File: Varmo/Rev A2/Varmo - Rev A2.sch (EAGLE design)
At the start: 110 parts, among them J1 22-05-7028-02, J2 22-05-7028-02, J3 22-05-7038-03, J4 22-05-7038-03, J5 22-05-7038-03, J6 22-05-7038-03, J7 22-05-7058-05, J9 22-05-7038-03, T1 MMBT2222AL, U1 LT1813CS8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

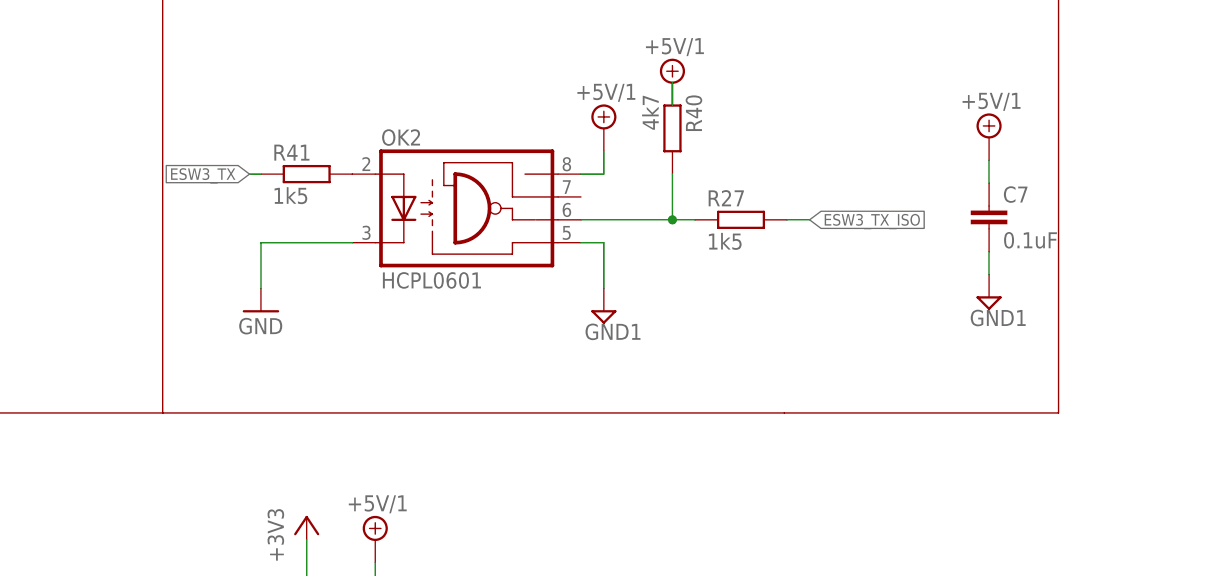
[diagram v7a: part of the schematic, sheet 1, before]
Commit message: Replace the HCPL0601 with the HCPL0201 optocoupler
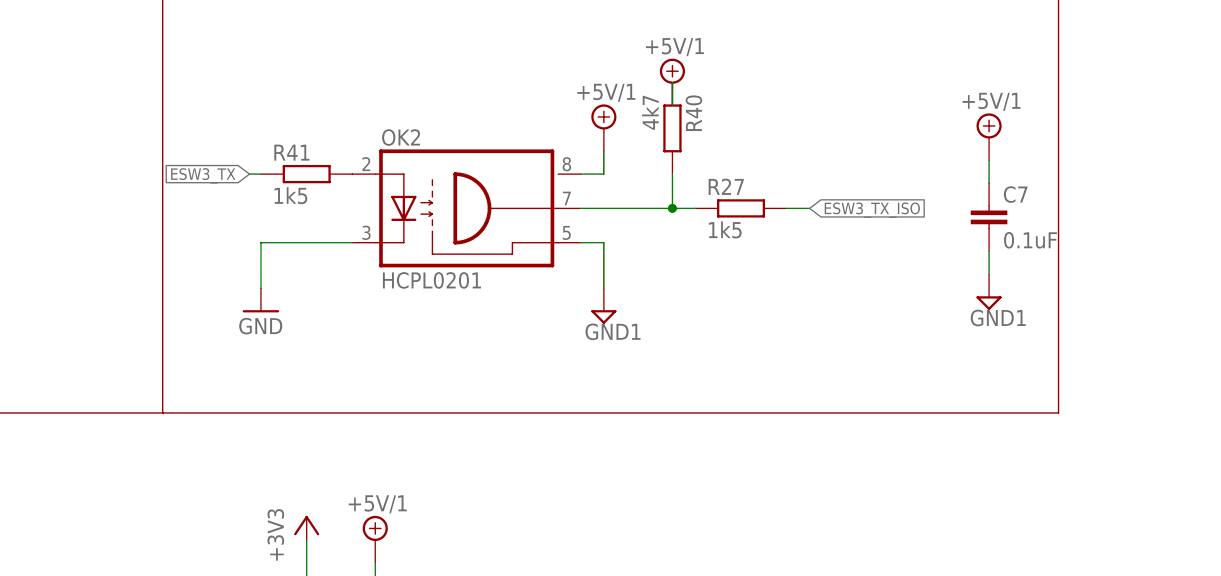
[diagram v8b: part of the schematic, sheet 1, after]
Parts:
- OK2: value HCPL0601 -> HCPL0201; device optocoupler:HCPL0601 -> optocoupler:HCPL0201
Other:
- moved on the sheet: R27
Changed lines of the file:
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@@
 <?xml version="1.0" encoding="utf-8"?>
 <!DOCTYPE eagle SYSTEM "eagle.dtd">
-<eagle version="7.5.0">
+<eagle version="7.6.0">
 <drawing>
 <settings>
@@
 <setting verticaltext="up"/>
 </settings>
-<grid distance="0.1" unitdist="inch" unit="inch" style="lines" multiple="1" display="no" altdistance="0.01" altunitdist="inch" altunit="inch"/>
+<grid distance="0.1" unitdist="inch" unit="inch" style="lines" multiple="1" display="no" altdistance="0.05" altunitdist="inch" altunit="inch"/>
 <layers>
 <layer number="1" name="Top" color="4" fill="1" visible="no" active="no"/>
@@
 </part>
 <part name="SUPPLY59" library="supply2" deviceset="+5V/1" device=""/>
-<part name="OK2" library="optocoupler" deviceset="HCPL0601" device=""/>
+<part name="OK2" library="optocoupler" deviceset="HCPL0201" device=""/>
 <part name="R41" library="rcl" deviceset="R-EU_" device="R0603" value="1k5">
 <attribute name="MF" value=""/>
@@
 <text x="113.64" y="197.58" size="1.778" layer="97">SIGNAL ISOLATION</text>
 <text x="105.38" y="252.38" size="1.778" layer="97">DC-DC convertor</text>
-<wire x1="169.92" y1="103" x2="100.84" y2="103" width="0.1524" layer="94"/>
+<wire x1="200.38" y1="103" x2="100.84" y2="103" width="0.1524" layer="94"/>
 <wire x1="100.84" y1="103" x2="3.746" y2="103" width="0.1524" layer="94"/>
 <wire x1="100.84" y1="103" x2="100.84" y2="202" width="0.1524" layer="94"/>
@@
 <wire x1="200.38" y1="202" x2="200.38" y2="182.92" width="0.1524" layer="94"/>
 <wire x1="200.38" y1="182.92" x2="200.38" y2="103" width="0.1524" layer="94"/>
-<wire x1="200.38" y1="103" x2="169.92" y2="103" width="0.1524" layer="94"/>
 <wire x1="383.492" y1="182.92" x2="200.38" y2="182.92" width="0.1524" layer="94"/>
 <text x="113.64" y="197.58" size="1.778" layer="97">SIGNAL ISOLATION</text>
@@
 </instance>
 <instance part="SUPPLY59" gate="G$1" x="157.48" y="139.7"/>
-<instance part="OK2" gate="A" x="134.62" y="124.46"/>
+<instance part="OK2" gate="G$1" x="134.62" y="124.46"/>
 <instance part="R41" gate="G$1" x="116.84" y="129.54">
 <attribute name="OC_NEWARK" x="116.84" y="129.54" size="1.778" layer="96" rot="R90" display="off"/>
@@
 <instance part="SUPPLY65" gate="G$1" x="309.88" y="246.38"/>
 <instance part="SUPPLY66" gate="G$1" x="355.6" y="246.38"/>
-<instance part="R27" gate="G$1" x="165.1" y="124.46">
-<attribute name="OC_NEWARK" x="165.1" y="124.46" size="1.778" layer="96" rot="R90" display="off"/>
-<attribute name="MF" x="165.1" y="124.46" size="1.778" layer="96" rot="R90" display="off"/>
-<attribute name="MPN" x="165.1" y="124.46" size="1.778" layer="96" rot="R90" display="off"/>
+<instance part="R27" gate="G$1" x="165.1" y="125.73">
+<attribute name="OC_NEWARK" x="165.1" y="125.73" size="1.778" layer="96" rot="R90" display="off"/>
+<attribute name="MF" x="165.1" y="125.73" size="1.778" layer="96" rot="R90" display="off"/>
+<attribute name="MPN" x="165.1" y="125.73" size="1.778" layer="96" rot="R90" display="off"/>
 </instance>
 <instance part="U8" gate="G$1" x="81.28" y="53.34"/>
@@
 </segment>
 <segment>
-<pinref part="OK2" gate="A" pin="C"/>
+<pinref part="OK2" gate="G$1" pin="C"/>
 <wire x1="111.76" y1="116.84" x2="111.76" y2="121.92" width="0.1524" layer="91"/>
 <wire x1="111.76" y1="121.92" x2="121.92" y2="121.92" width="0.1524" layer="91"/>
@@
 <segment>
 <pinref part="SUPPLY11" gate="G$1" pin="GND1"/>
-<pinref part="OK2" gate="A" pin="GND"/>
+<pinref part="OK2" gate="G$1" pin="GND"/>
 <wire x1="149.86" y1="116.84" x2="149.86" y2="121.92" width="0.1524" layer="91"/>
 <wire x1="149.86" y1="121.92" x2="147.32" y2="121.92" width="0.1524" layer="91"/>
@@
 </segment>
 <segment>
-<pinref part="OK2" gate="A" pin="VCC"/>
+<pinref part="OK2" gate="G$1" pin="VCC"/>
 <pinref part="SUPPLY10" gate="G$1" pin="+5V/1"/>
 <wire x1="147.32" y1="129.54" x2="149.86" y2="129.54" width="0.1524" layer="91"/>
@@
 <segment>
 <pinref part="R27" gate="G$1" pin="2"/>
-<wire x1="170.18" y1="124.46" x2="172.72" y2="124.46" width="0.1524" layer="91"/>
-<label x="172.72" y="124.46" size="1.27" layer="95" xref="yes"/>
+<wire x1="170.18" y1="125.73" x2="172.72" y2="125.73" width="0.1524" layer="91"/>
+<label x="172.72" y="125.73" size="1.27" layer="95" xref="yes"/>
 </segment>
 <segment>
@@
 <segment>
 <pinref part="R41" gate="G$1" pin="2"/>
-<pinref part="OK2" gate="A" pin="A"/>
+<pinref part="OK2" gate="G$1" pin="A"/>
 </segment>
 </net>
@@
 <net name="N$15" class="0">
 <segment>
-<pinref part="OK2" gate="A" pin="VO"/>
+<pinref part="OK2" gate="G$1" pin="VO"/>
 <pinref part="R27" gate="G$1" pin="1"/>
-<wire x1="147.32" y1="124.46" x2="157.48" y2="124.46" width="0.1524" layer="91"/>
+<wire x1="147.32" y1="125.73" x2="157.48" y2="125.73" width="0.1524" layer="91"/>
 <pinref part="R40" gate="G$1" pin="2"/>
-<wire x1="157.48" y1="124.46" x2="160.02" y2="124.46" width="0.1524" layer="91"/>
-<wire x1="157.48" y1="129.54" x2="157.48" y2="124.46" width="0.1524" layer="91"/>
-<junction x="157.48" y="124.46"/>
-</segment>
-</net>
+<wire x1="157.48" y1="125.73" x2="160.02" y2="125.73" width="0.1524" layer="91"/>
+<wire x1="157.48" y1="129.54" x2="157.48" y2="125.73" width="0.1524" layer="91"/>
+<junction x="157.48" y="125.73"/>
+</segment>
+</net>
